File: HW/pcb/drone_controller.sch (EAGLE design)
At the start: 29 parts, among them IC2 MEGA8-P, J1 DCJ0202, Q1 16Mhz, U1 ICM-20600

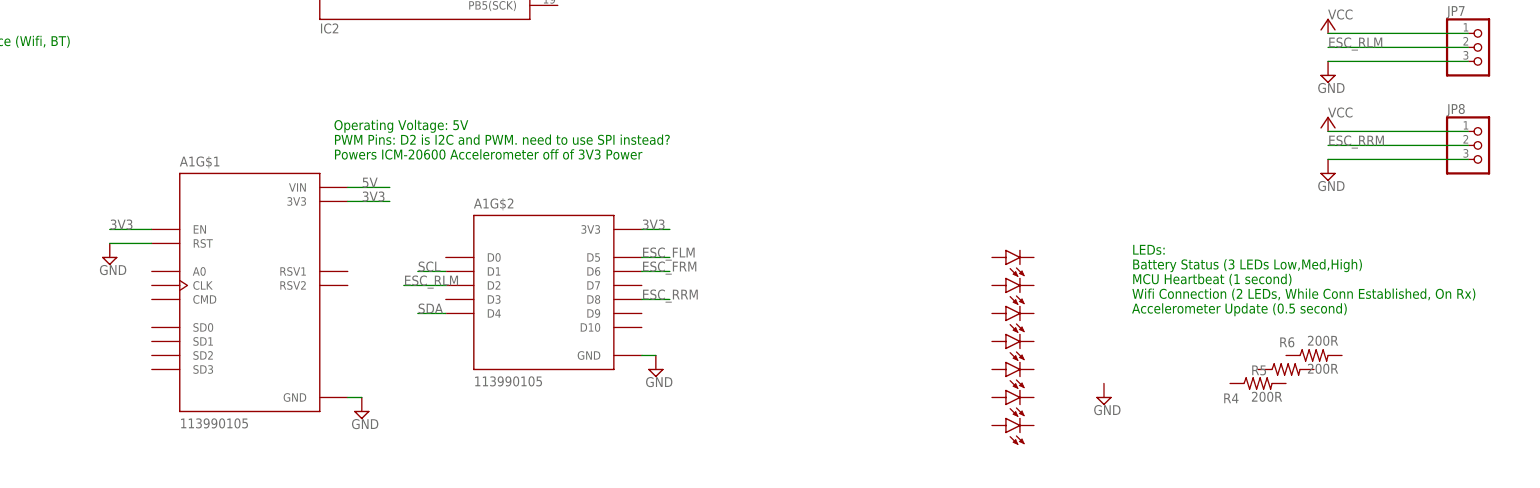
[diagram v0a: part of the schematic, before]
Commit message: implemented heartbeat LED in SW. Adjusted position of MCU on board to account for loss from GND plane. Removed unneeded battery indicators (only one LED for Low BATT).
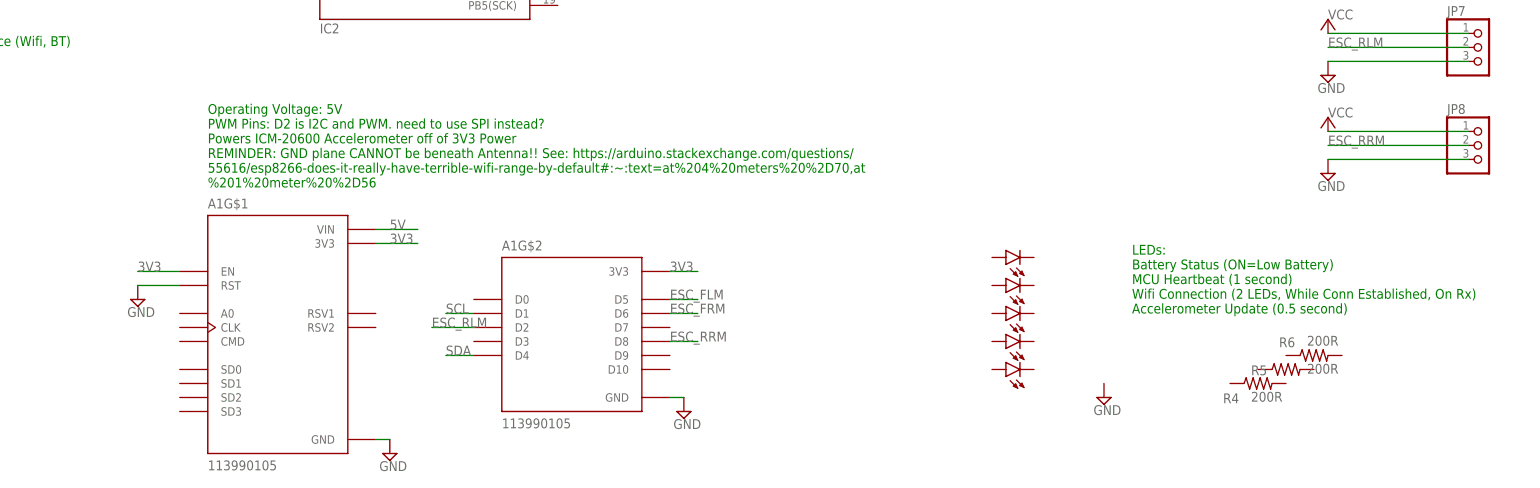
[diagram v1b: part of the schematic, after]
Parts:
- removed LED1, LED7: (no value), led:LED5MM
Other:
- note added: "LEDs: Battery Status (ON=Low Battery) MCU Heartbeat (1 second) Wifi Connection (2 LEDs, While Conn Established, On Rx) Accelerometer Update (0.5 second)"
- note added: "Operating Voltage: 5V PWM Pins: D2 is I2C and PWM. need to use SPI instead? Powers ICM-20600 Accelerometer off of 3V3 Power REMINDER: GND plane CANNOT be beneath Antenna!! See: https://arduino.stackexchange.com/questions/ 55616/esp8266-does-it-really-have-terrible-wifi-range-by-default#:~:text=at%204%20meters%20%2D70,at %201%20meter%20%2D56"
- note removed: "LEDs: Battery Status (3 LEDs Low,Med,High) MCU Heartbeat (1 second) Wifi Connection (2 LEDs, While Conn Established, On Rx) Accelerometer Update (0.5 second)"
- note removed: "Operating Voltage: 5V PWM Pins: D2 is I2C and PWM. need to use SPI instead? Powers ICM-20600 Accelerometer off of 3V3 Power"
- moved on the sheet: A1G$1, A1G$2

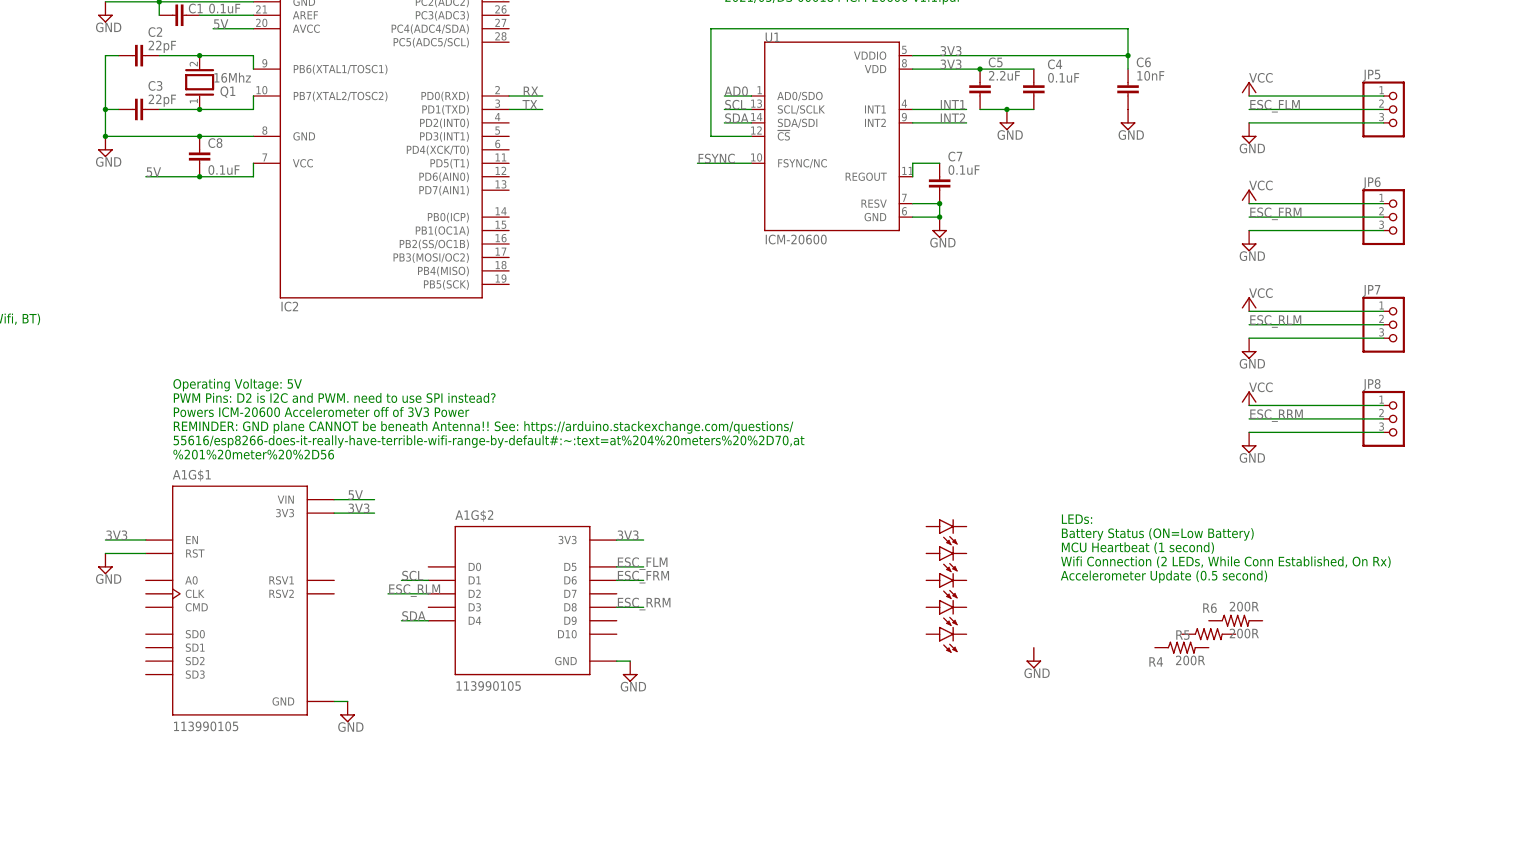
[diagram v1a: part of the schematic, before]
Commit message: implemented pinout into schematic. added LED interface
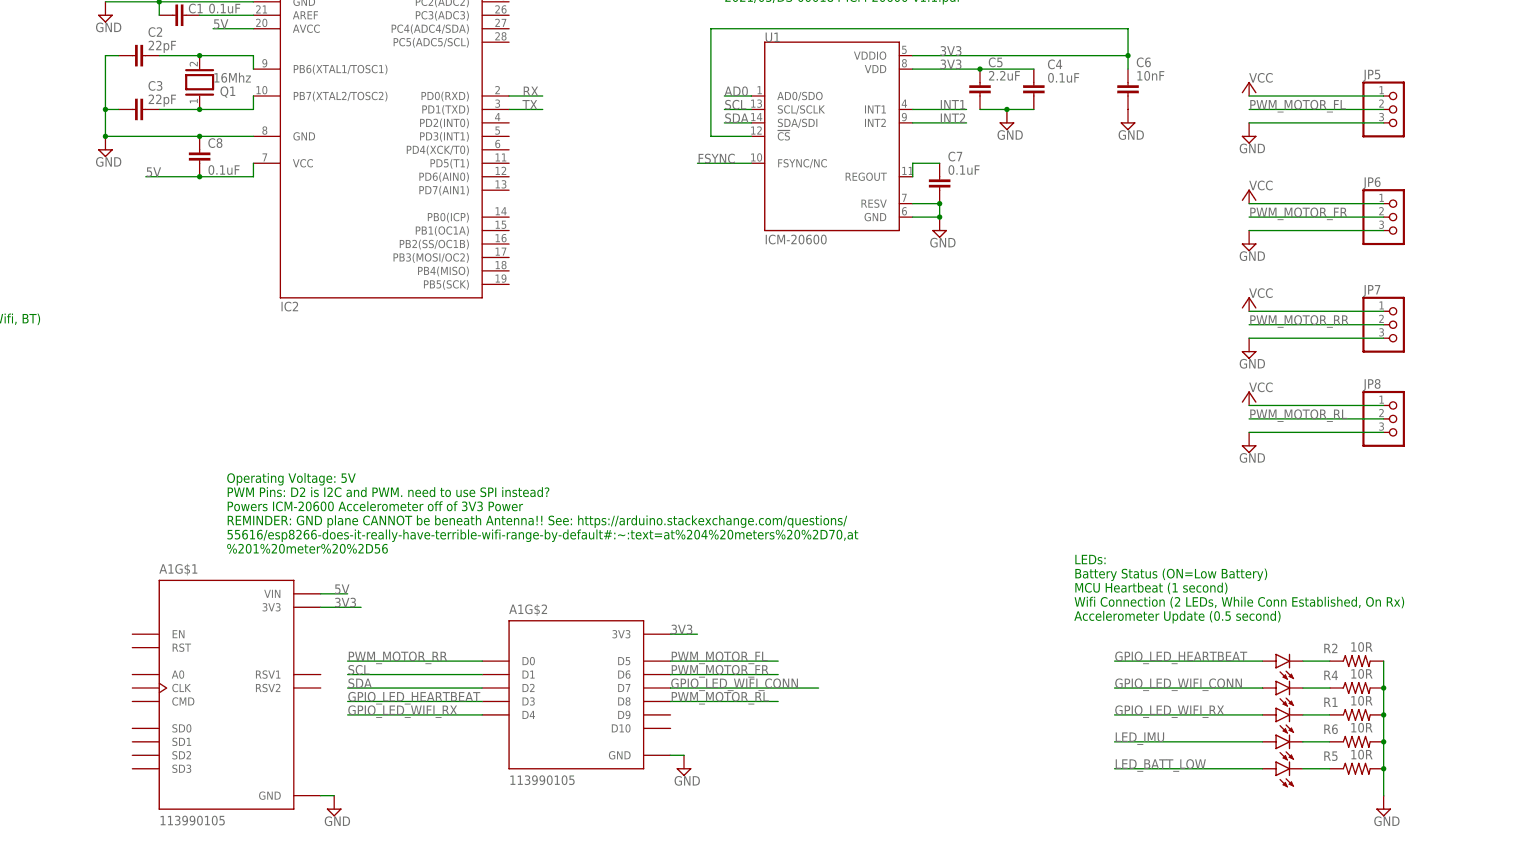
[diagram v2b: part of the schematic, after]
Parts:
- added R1, R2: 10R, rcl:R-US_0411/12
- R4, R5, R6: value 200R -> 10R
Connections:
- net ESC_FLM renamed PWM_MOTOR_FL
- net ESC_FRM renamed PWM_MOTOR_FR
- net ESC_RRM renamed PWM_MOTOR_RL
- removed net ESC_RLM: A1G$2.D2, JP7.2
- new net GPIO_LED_HEARTBEAT: A1G$2.D3, LED4.A
- new net GPIO_LED_WIFI_CONN: A1G$2.D7, LED5.A
- new net GPIO_LED_WIFI_RX: A1G$2.D4, LED6.A
- new net LED_BATT_LOW: LED3.A
- new net LED_IMU: LED2.A
- new net N$10: LED4.C, R2.1
- new net N$14: LED6.C, R1.1
- new net N$7: LED2.C, R6.1
- new net N$8: LED3.C, R5.1
- new net N$9: LED5.C, R4.1
- new net PWM_MOTOR_RR: A1G$2.D0, JP7.2
- net 3V3: no longer A1G$1.EN
- net GND: now also R1.2, R2.2, R4.2, R5.2, R6.2; no longer A1G$1.RST
- net SDA: now also A1G$2.D2; no longer A1G$2.D4
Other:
- moved on the sheet: A1G$1, A1G$2, R4, R5, R6

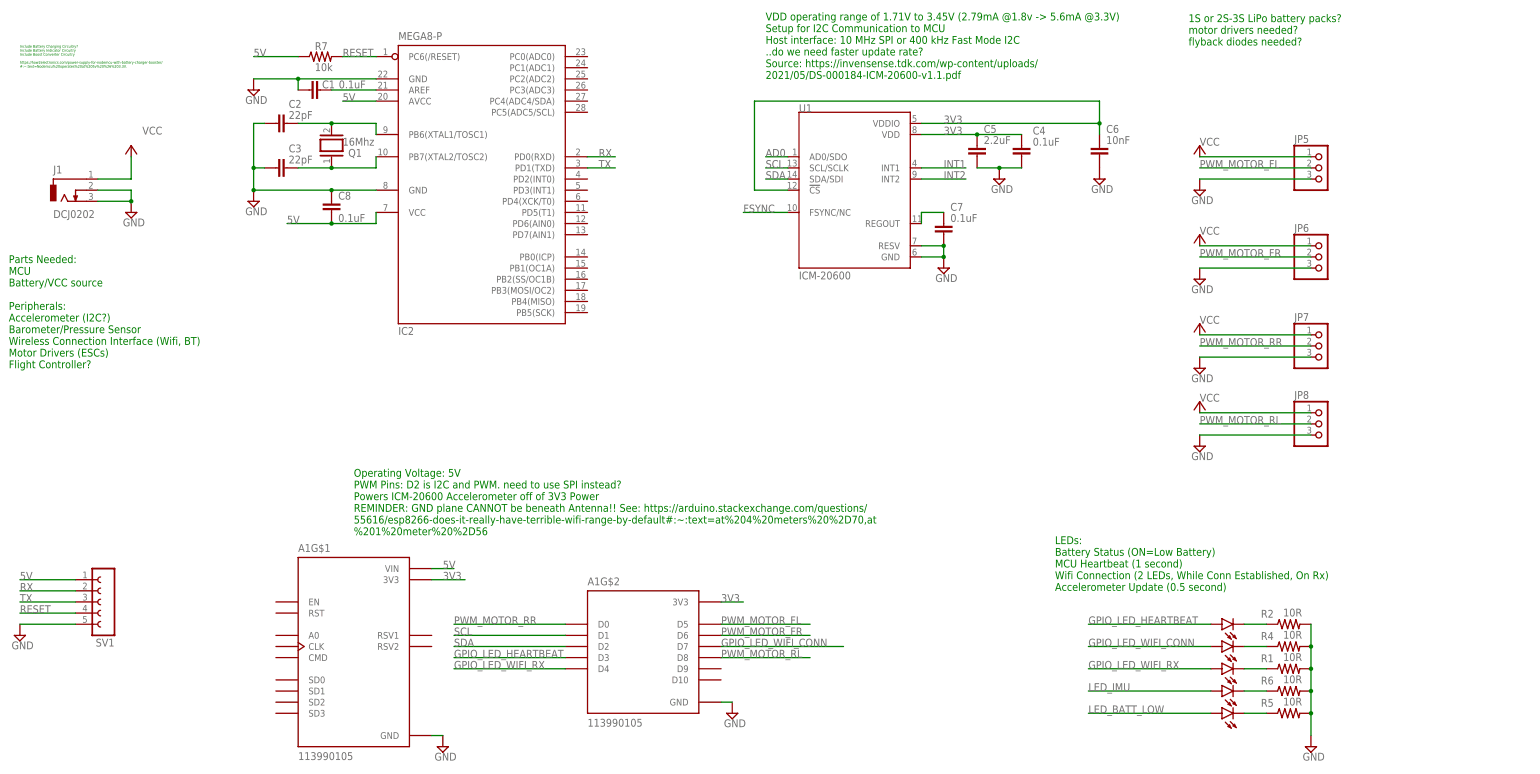
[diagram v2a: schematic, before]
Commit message: working on PCB design. added 3.3v to 5v level shifter, but it is not needed. tested NodeMCU to SpeedyBee ESC and was able to communicate using Servo Library without needed PWM voltage to increase from 3.3v to 5v. 3.3 worked fine.
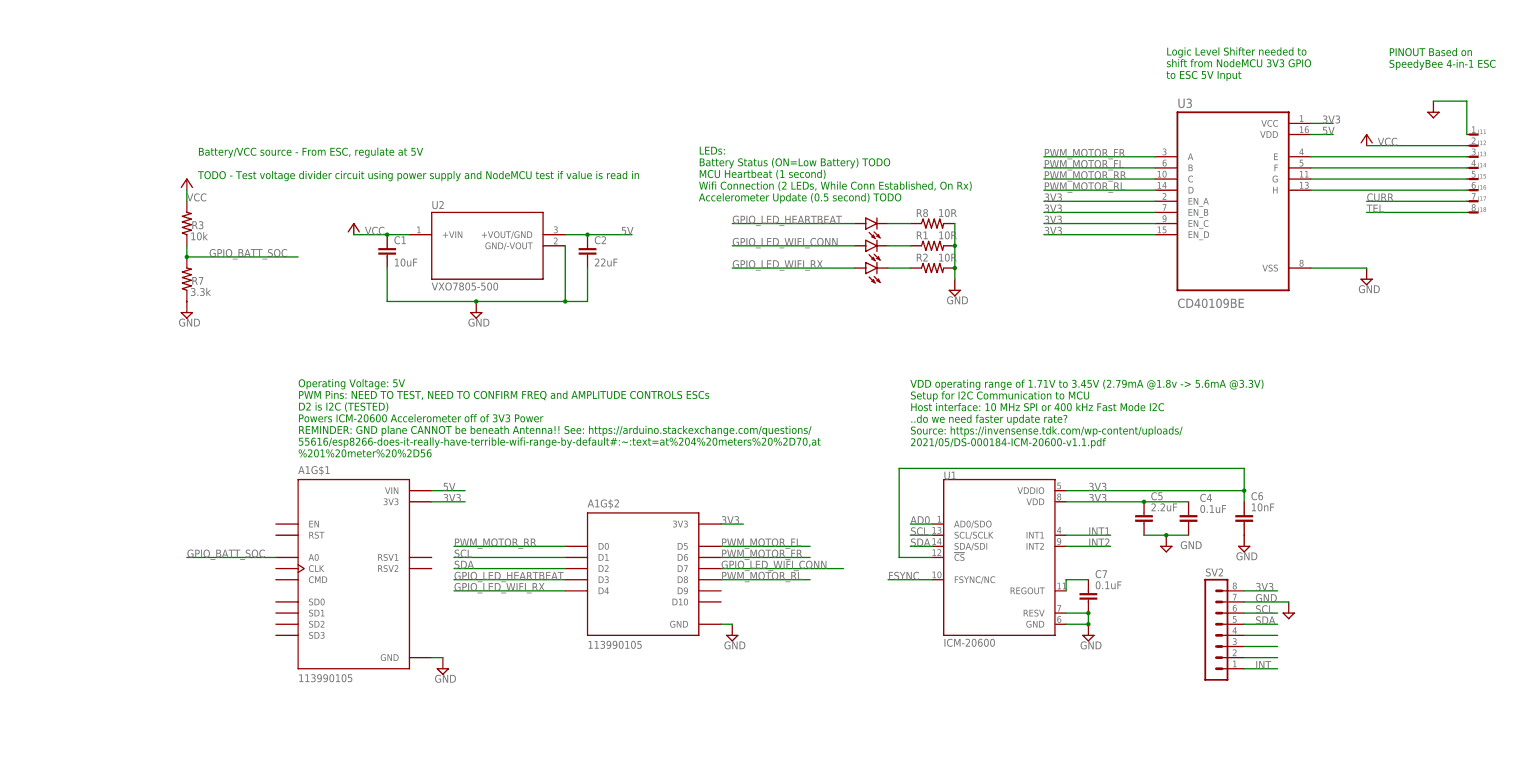
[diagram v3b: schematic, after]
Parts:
- removed C3: 22pF, capacitor-wima:C2,5-3
- removed C8: 0.1uF, capacitor-wima:C2,5-3
- removed IC2: MEGA8-P, atmel:MEGA8-P
- removed JP5, JP6, JP7, JP8: (no value), pinhead:PINHD-1X3
- removed LED2, LED3: (no value), led:LED5MM
- removed Q1: 16Mhz, special:XTAL/S
- removed R4, R5, R6: 10R, rcl:R-US_0411/12
- removed SV1: (no value), con-lsta:FE05-1
- added R3: 10k, rcl:R-US_0204/7
- added R8: 10R, rcl:R-US_0204/7
- added SV2: (no value), con-lstb:MA08-1
- added U2: VXO7805-500, VXO7805-500:VXO7805-500
- added U3: CD40109BE, CD40109BE:CD40109BE
- C1: value 0.1uF -> 10uF
- C2: value 22pF -> 22uF
- J1: value DCJ0202 -> SM08B-SRSS-TB; device con-jack:DCJ0202 -> con-JST-SH:SM08B-SRSS-TB
- R1, R2: device rcl:R-US_0411/12 -> rcl:R-US_0204/7
- R7: value 10k -> 3.3k; device rcl:R-US_0207/10 -> rcl:R-US_0204/7
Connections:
- removed net LED_BATT_LOW: LED3.A
- removed net LED_IMU: LED2.A
- removed net N$12: C2.1, IC2.PB6(XTAL1/TOSC1), Q1.2
- removed net N$13: C1.1, IC2.AREF
- removed net N$7: LED2.C, R6.1
- removed net N$8: LED3.C, R5.1
- removed net RESET: IC2.PC6(/RESET), R7.2, SV1.4
- removed net RX: IC2.PD0(RXD), SV1.2
- removed net TX: IC2.PD1(TXD), SV1.3
- new net CURR: J17.P
- new net GPIO_BATT_SOC: A1G$1.A0, R3.1, R7.2
- new net INT: SV2.1
- new net N$17: SV2.4
- new net N$18: SV2.3
- new net N$19: SV2.2
- new net N$2: J13.P, U3.E
- new net N$3: J14.P, U3.F
- new net N$4: J15.P, U3.G
- new net TEL: J18.P
- net 3V3: now also SV2.8, U3.EN_A, U3.EN_B, U3.EN_C, U3.EN_D, U3.VCC
- net 5V: now also C2.1, U2.+VOUT/GND, U3.VDD; no longer C8.2, IC2.AVCC, IC2.VCC@1, R7.1, SV1.1
- net GND: now also J11.P, R7.1, R8.2, SV2.7, U2.GND/-VOUT, U3.VSS; no longer C3.2, C8.1, IC2.GND, IC2.GND@1, J1.2, J1.3, JP5.3, JP6.3, JP7.3, JP8.3, R4.2, R5.2, R6.2, SV1.5
- net N$10: now also R8.1; no longer R2.1
- net N$11: now also J16.P, U3.H; no longer C3.1, IC2.PB7(XTAL2/TOSC2), Q1.1
- net N$14: now also R2.1; no longer R1.1
- net N$9: now also R1.1; no longer R4.1
- net PWM_MOTOR_FL: now also U3.B; no longer JP5.2
- net PWM_MOTOR_FR: now also U3.A; no longer JP6.2
- net PWM_MOTOR_RL: now also U3.D; no longer JP8.2
- net PWM_MOTOR_RR: now also U3.C; no longer JP7.2
- net SCL: now also SV2.6
- net SDA: now also SV2.5
- net VCC: now also C1.1, J12.P, R3.2, U2.+VIN; no longer J1.1, JP5.1, JP6.1, JP7.1, JP8.1
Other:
- note added: "Battery/VCC source - From ESC, regulate at 5V TODO - Test voltage divider circuit using power supply and NodeMCU test if value is read in"
- note added: "LEDs: Battery Status (ON=Low Battery) TODO MCU Heartbeat (1 second) Wifi Connection (2 LEDs, While Conn Established, On Rx) Accelerometer Update (0.5 second) TODO"
- note added: "Logic Level Shifter needed to shift from NodeMCU 3V3 GPIO to ESC 5V Input"
- note added: "Operating Voltage: 5V PWM Pins: NEED TO TEST, NEED TO CONFIRM FREQ and AMPLITUDE CONTROLS ESCs D2 is I2C (TESTED) Powers ICM-20600 Accelerometer off of 3V3 Power REMINDER: GND plane CANNOT be beneath Antenna!! See: https://arduino.stackexchange.com/questions/ 55616/esp8266-does-it-really-have-terrible-wifi-range-by-default#:~:text=at%204%20meters%20%2D70,at %201%20meter%20%2D56"
- note added: "PINOUT Based on SpeedyBee 4-in-1 ESC"
- note removed: "1S or 2S-3S LiPo battery packs? motor drivers needed? flyback diodes needed?"
- note removed: "Include Battery Charging Circuitry? Include Battery Indicator Circuitry Include Boost Converter Circuitry https://how2electronics.com/power-supply-for-nodemcu-with-battery-charger-booster/ #:~:text=Nodemcu%20operates%20at%205v%20%26%203.3V."
- note removed: "LEDs: Battery Status (ON=Low Battery) MCU Heartbeat (1 second) Wifi Connection (2 LEDs, While Conn Established, On Rx) Accelerometer Update (0.5 second)"
- note removed: "Operating Voltage: 5V PWM Pins: D2 is I2C and PWM. need to use SPI instead? Powers ICM-20600 Accelerometer off of 3V3 Power REMINDER: GND plane CANNOT be beneath Antenna!! See: https://arduino.stackexchange.com/questions/ 55616/esp8266-does-it-really-have-terrible-wifi-range-by-default#:~:text=at%204%20meters%20%2D70,at %201%20meter%20%2D56"
- note removed: "Parts Needed: MCU Battery/VCC source Peripherals: Accelerometer (I2C?) Barometer/Pressure Sensor Wireless Connection Interface (Wifi, BT) Motor Drivers (ESCs) Flight Controller?"
- moved on the sheet: A1G$1, A1G$2, C1, C2, C4, C5, C6, C7, R1, R2, R7, U1
